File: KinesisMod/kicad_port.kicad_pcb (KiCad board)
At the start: 2 copper layers, 100 x 86 mm, 17 parts, among them J1 Conn_01x13, J2 Conn_01x13, J3 Conn_01x13, J4 Conn_01x13, J5 Conn_01x10, J6 Conn_01x10, U1 Teensy++_2_0

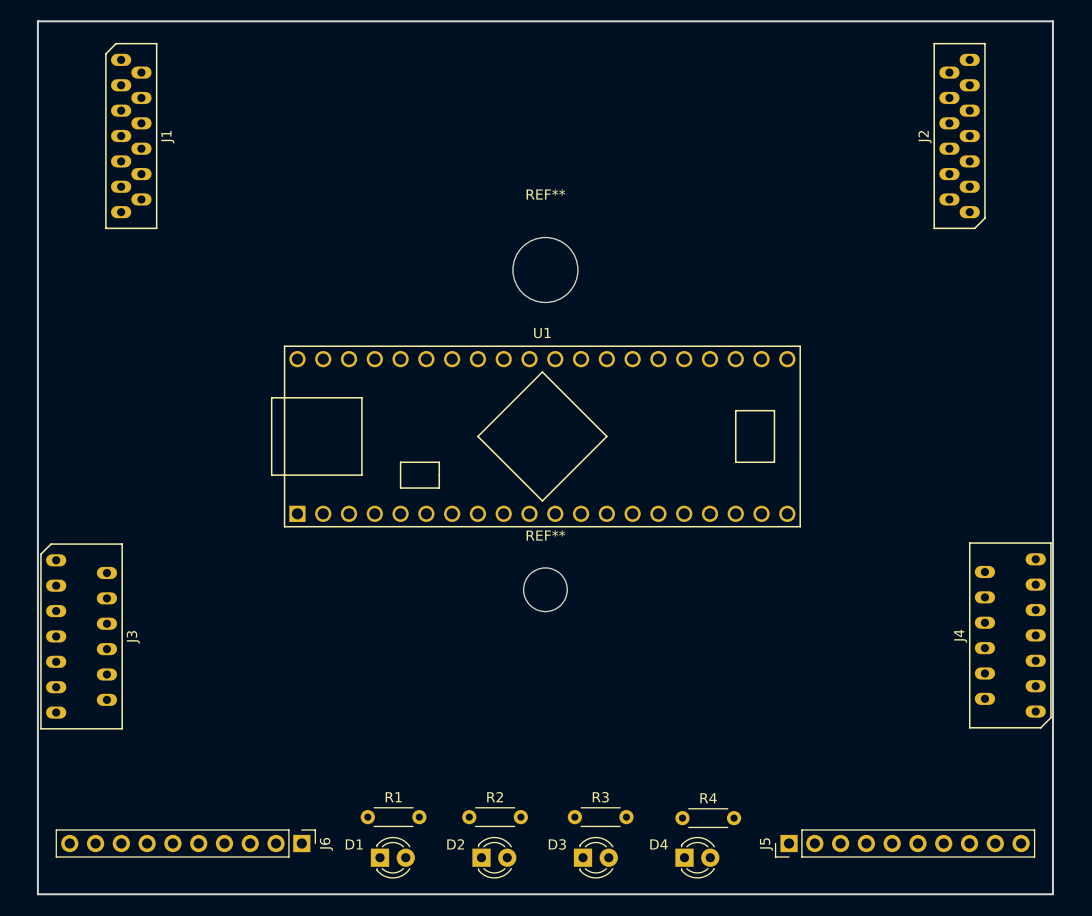
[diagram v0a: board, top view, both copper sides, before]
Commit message: first pass auto-routed with FreeRouting.jar, should probably re-orient some stuff (LEDS) and do another pass. Board has been 3D printed and checked for size compatibility with case and keywells
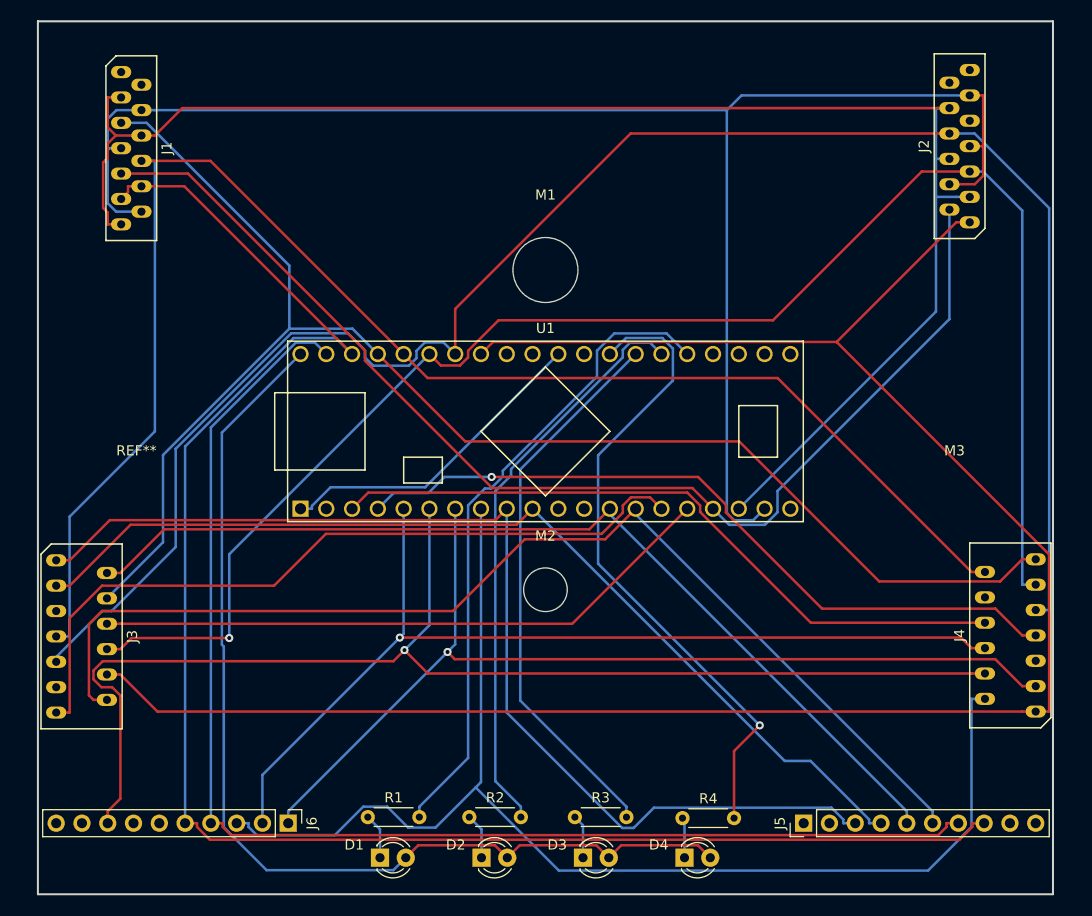
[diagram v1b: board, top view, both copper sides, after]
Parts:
- added M3: MountingHole_4.3mm_M4, MountingHole:MountingHole_4.3mm_M4, F.Cu at (190.3, 97.6)
- added REF**: MountingHole_4.3mm_M4, MountingHole:MountingHole_4.3mm_M4, F.Cu at (109.7, 97.6)
- moved J5 2.46 mm to (175.4, 129.0)
- moved J6 2.41 mm to (124.7, 129.0)
- moved J1 1.20 mm to (109.2, 62.5)
- moved J2 1.00 mm to (190.8, 62.3)
- moved U1 0.58 mm to (150.0, 90.4)
- renumbered REF** to M1, REF** to M2
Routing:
- net /PB0: track 0.00 -> 192.9 mm
- net /PB1: track 0.00 -> 176.3 mm
- net /PB5: track 0.00 -> 169.6 mm
- net /PC6: track 0.00 -> 157.6 mm
- net /PB2: track 0.00 -> 155.6 mm, vias 0 -> 1
- net /PC5: track 0.00 -> 153.0 mm
- net /PB3: track 0.00 -> 152.9 mm
- net /PB4: track 0.00 -> 147.4 mm
- net /PB6: track 0.00 -> 129.3 mm
- net /PD5: track 0.00 -> 123.5 mm
- net /PD3: track 0.00 -> 121.8 mm, vias 0 -> 1
- net /PC4: track 0.00 -> 116.9 mm
- net /PC1: track 0.00 -> 110.6 mm
- net /PD6: track 0.00 -> 107.3 mm
- net +5V: track 0.00 -> 103.1 mm
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
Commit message: re-routed with LEDs flipped onto other side of board
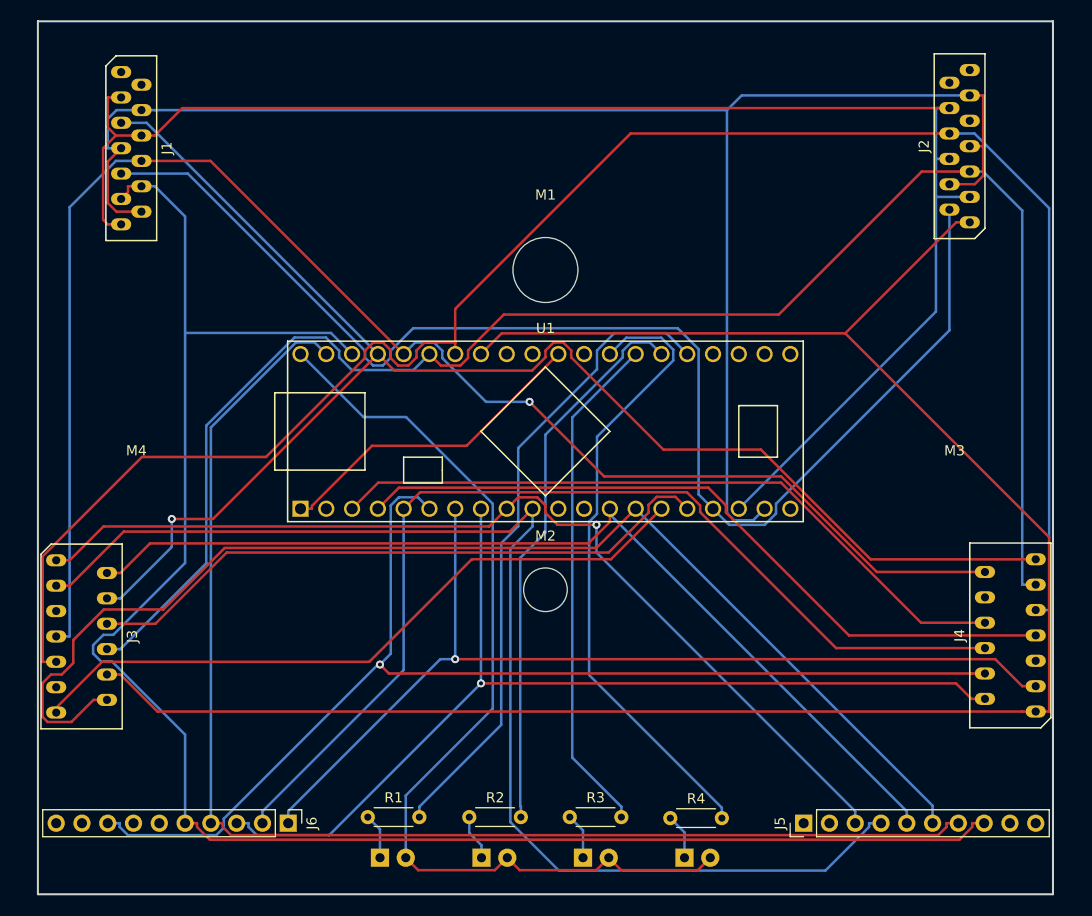
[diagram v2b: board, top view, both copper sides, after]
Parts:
- D1, D2, D3, D4: moved to B.Cu
- moved R4 1.20 mm to (162.3, 128.5)
- moved R3 0.50 mm to (152.4, 128.4)
- renumbered REF** to M4
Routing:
- net /PD5: track 123.5 -> 98.5 mm, vias 0 -> 1
- net /PD7: track 97.4 -> 122.5 mm
- net /PC4: track 116.9 -> 128.5 mm
- net /PC1: track 110.6 -> 120.8 mm
- net /PD6: track 107.3 -> 97.3 mm, vias 0 -> 1
- net +5V: track 103.1 -> 96.5 mm
- net /PD2: track 94.8 -> 101.4 mm, vias 1 -> 0
- net /PC2: track 74.8 -> 68.2 mm
- net /PB2: track 155.6 -> 161.8 mm, vias 1 -> 0
- net /PD3: track 121.8 -> 115.7 mm
- net /PB5: track 169.6 -> 174.7 mm
- net /PF1: track 54.7 -> 50.2 mm
- net /PF2: track 56.8 -> 54.8 mm
- net /PB1: track 176.3 -> 178.3 mm
- net /PB4: track 147.4 -> 149.3 mm, vias 0 -> 1
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
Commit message: realized J1 and J2 were swapped and J3 and J4 were swapped. Replced and re-routed
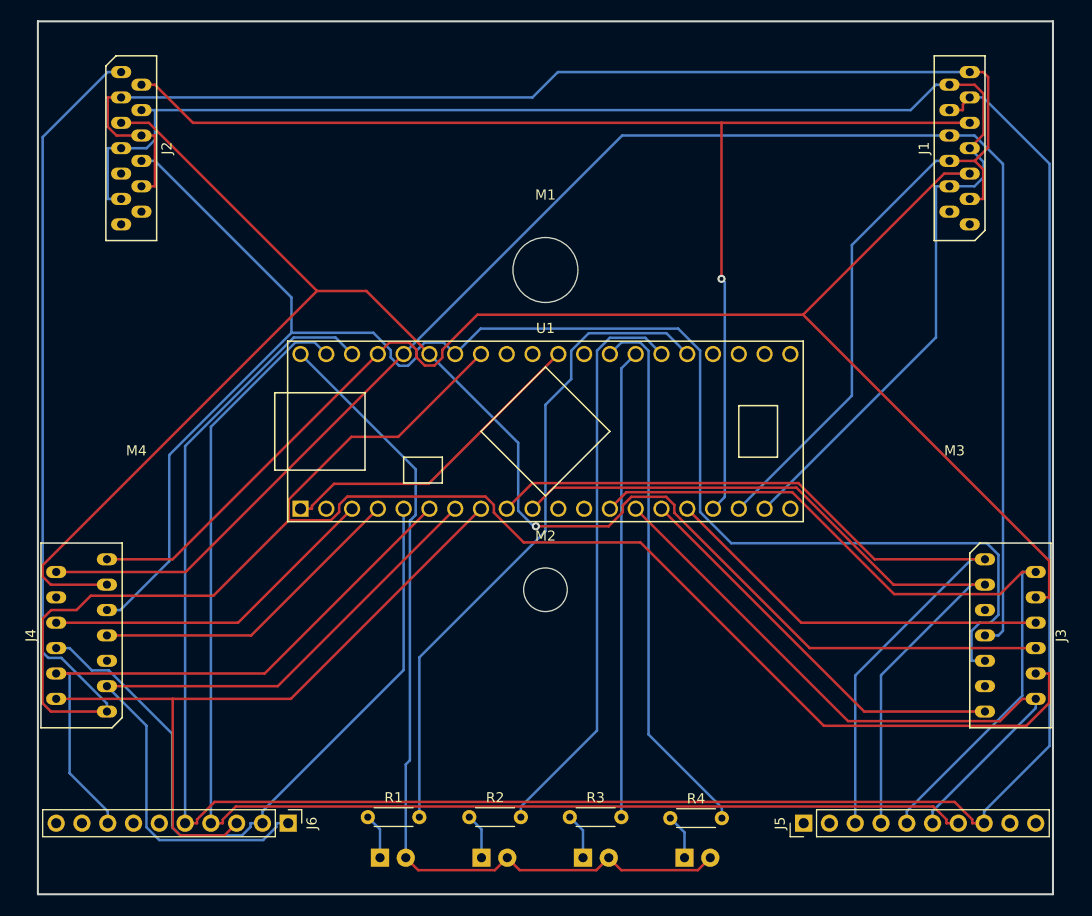
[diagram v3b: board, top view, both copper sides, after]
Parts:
- moved J3 91.5 mm to (195.8, 110.5)
- moved J4 91.5 mm to (104.3, 110.5)
- moved J2 81.6 mm to (109.2, 62.5), turned to 270 degrees
- moved J1 81.6 mm to (190.8, 62.5), turned to 90 degrees
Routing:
- net /PC1: track 120.8 -> 65.4 mm
- net /PD3: track 115.7 -> 61.1 mm, vias 1 -> 0
- net /PB5: track 174.7 -> 220.7 mm
- net /PD7: track 122.5 -> 77.9 mm
- net /PD1: track 72.1 -> 31.9 mm
- net /PB0: track 193.4 -> 231.8 mm
- net /PD0: track 69.1 -> 33.8 mm
- net /PD2: track 101.4 -> 70.8 mm
- net /PD5: track 98.5 -> 69.4 mm, vias 1 -> 0
- net /PC2: track 68.2 -> 40.1 mm
- net /PD4: track 96.9 -> 72.5 mm, vias 1 -> 0
- net /PC3: track 63.3 -> 39.0 mm
- net /PC0: track 96.0 -> 78.5 mm
- net /PD6: track 97.3 -> 83.3 mm, vias 1 -> 0
- net /PB1: track 178.3 -> 165.7 mm
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
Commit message: parts were not on correct side of board, had to re-orient and re-route. In addition I added the 3d Models for the other parts
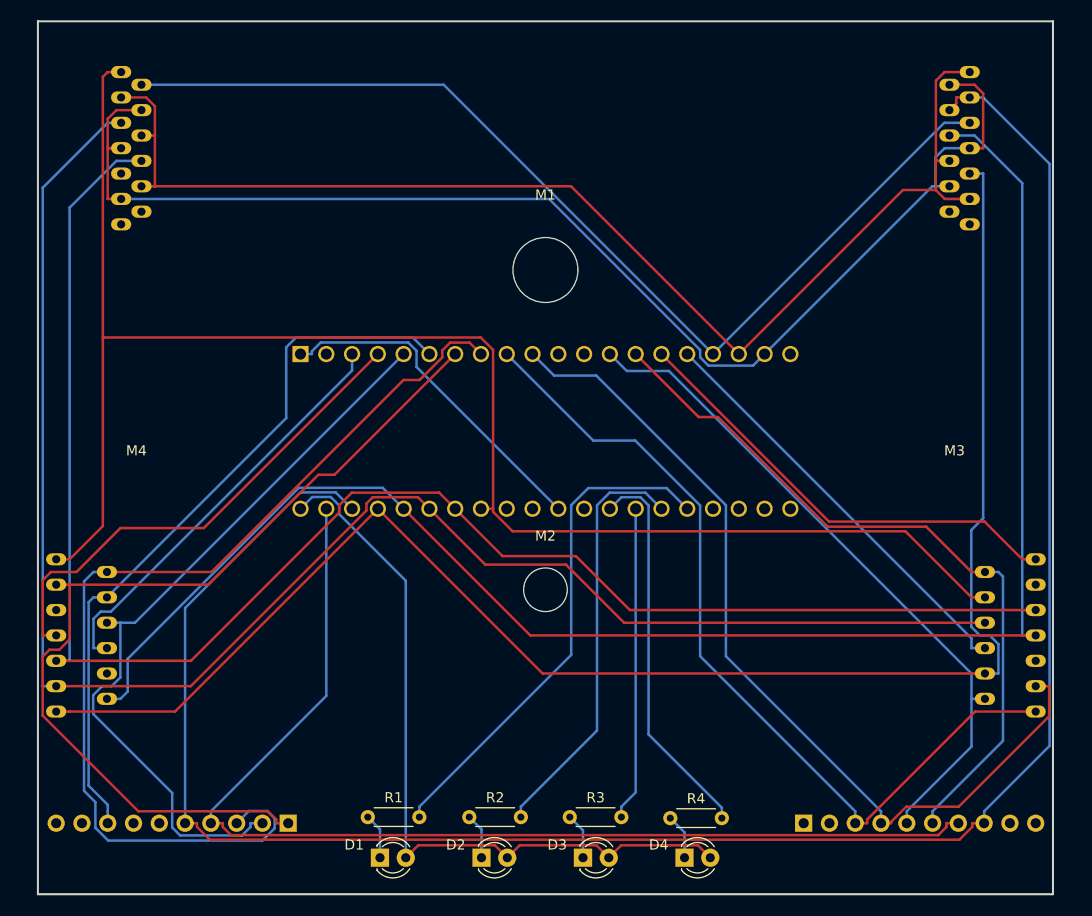
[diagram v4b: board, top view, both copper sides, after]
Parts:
- D1, D2, D3, D4: moved to F.Cu
- J1, J2, J3, J4, J5, J6, U1: moved to B.Cu
- turned J1 to 270 degrees
- turned J2 to 90 degrees
- turned J5 to 270 degrees
- turned J6 to 90 degrees
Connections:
- J1 pad 1: Net-(J1-Pad1) -> /PC5
- J1 pad 10: /PB5 -> /PC6
- J1 pad 11: /PB5 -> /PC5
- J1 pad 12: /PC6 -> Net-(J1-Pad12)
- J1 pad 13: /PC5 -> Net-(J1-Pad13)
- J1 pad 2: Net-(J1-Pad2) -> /PC6
- J1 pad 3: /PC5 -> /PB5
- J1 pad 4: /PC6 -> /PB5
- J1 pad 5: /PB4 -> /PC4
- J1 pad 6: /PC5 -> /PB3
- J1 pad 8: /PB3 -> /PC5
- J1 pad 9: /PC4 -> /PB4
- J2 pad 1: /PB0 -> Net-(J2-Pad1)
- J2 pad 10: /PC5 -> /PC6
- J2 pad 11: /PC6 -> /PC5
- J2 pad 12: Net-(J2-Pad12) -> /PC4
- J2 pad 13: Net-(J2-Pad13) -> /PB0
- J2 pad 2: /PC4 -> Net-(J2-Pad2)
- J2 pad 3: /PC5 -> /PC6
- J2 pad 4: /PC6 -> /PC5
- J2 pad 5: /PB2 -> Net-(J2-Pad5)
- J2 pad 6: /PC5 -> /PB1
- J2 pad 8: /PB1 -> /PC5
- J2 pad 9: Net-(J2-Pad9) -> /PB2
- J3 pad 1: /PD6 -> /PC2
- J3 pad 10: /PB0 -> /PB4
- J3 pad 11: Net-(J3-Pad11) -> /PD7
- J3 pad 12: /PC1 -> /PC0
- J3 pad 13: /PC2 -> /PD6
- J3 pad 2: /PC0 -> /PC1
- J3 pad 3: /PD7 -> Net-(J3-Pad3)
- J3 pad 4: /PB4 -> /PB0
- J3 pad 5: Net-(J3-Pad5) -> /PB1
- J3 pad 6: /PC3 -> /PB2
- J3 pad 8: /PB2 -> /PC3
- J3 pad 9: /PB1 -> Net-(J3-Pad9)
- J4 pad 1: /PB0 -> /PB4
- J4 pad 10: Net-(J4-Pad10) -> /PD3
- J4 pad 11: /PB2 -> /PD4
- J4 pad 12: /PB3 -> /PD5
- J4 pad 13: /PB4 -> /PB0
- J4 pad 2: /PD5 -> /PB3
- J4 pad 3: /PD4 -> /PB2
- J4 pad 4: /PD3 -> Net-(J4-Pad4)
- J4 pad 5: Net-(J4-Pad5) -> /PB1
- J4 pad 6: /PD2 -> /PD0
- J4 pad 8: /PD0 -> /PD2
- J4 pad 9: /PB1 -> Net-(J4-Pad9)
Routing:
- net /PB0: track 231.8 -> 160.2 mm
- net /PC5: track 162.6 -> 124.2 mm
- net /PD5: track 69.4 -> 98.7 mm
- net /PC6: track 151.8 -> 127.3 mm
- net /PC4: track 121.8 -> 102.0 mm, vias 1 -> 0
- net /PD4: track 72.5 -> 92.1 mm
- net /PB6: track 129.8 -> 110.7 mm
- net /PB4: track 142.7 -> 160.6 mm
- net /PD1: track 31.9 -> 49.0 mm
- net /PB5: track 220.7 -> 204.6 mm
- net /PF2: track 56.6 -> 41.3 mm
- net /PF0: track 53.7 -> 38.4 mm
- net /PF1: track 46.2 -> 31.0 mm
- net /PF3: track 65.1 -> 49.9 mm
- net +5V: track 87.8 -> 75.1 mm
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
